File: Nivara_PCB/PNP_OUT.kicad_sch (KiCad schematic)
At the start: 16 parts, among them Q3 IRLML0040, Q4 IRLML0040, U10 LTV-357T, U11 LTV-357T

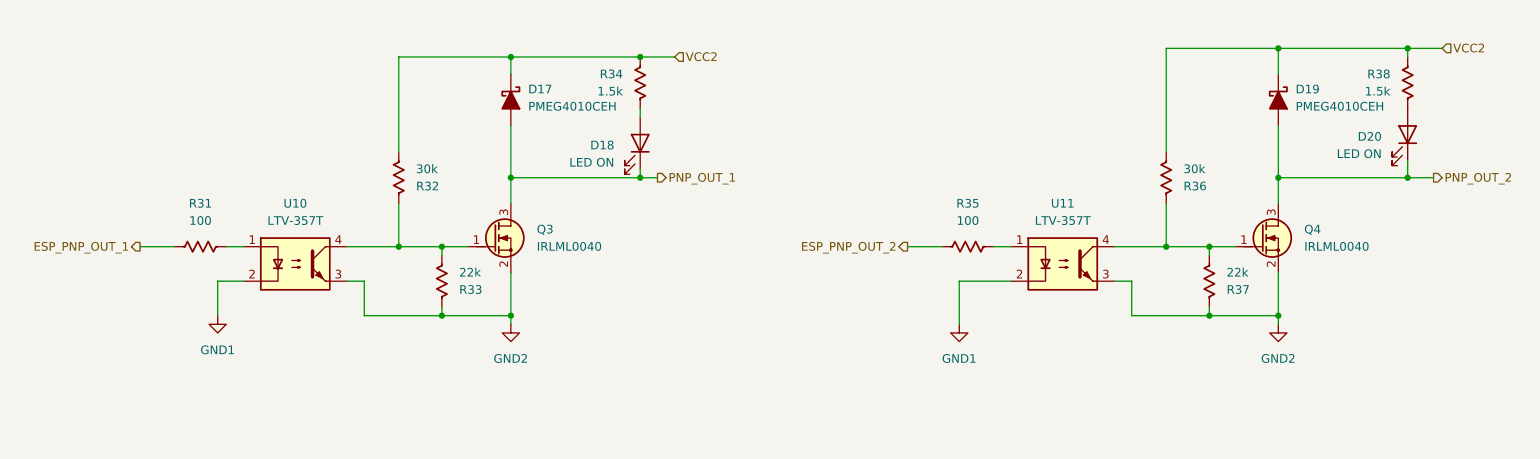
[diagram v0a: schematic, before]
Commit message: Cambios realizados en el PCB y el esquema de Nivara_PCB.
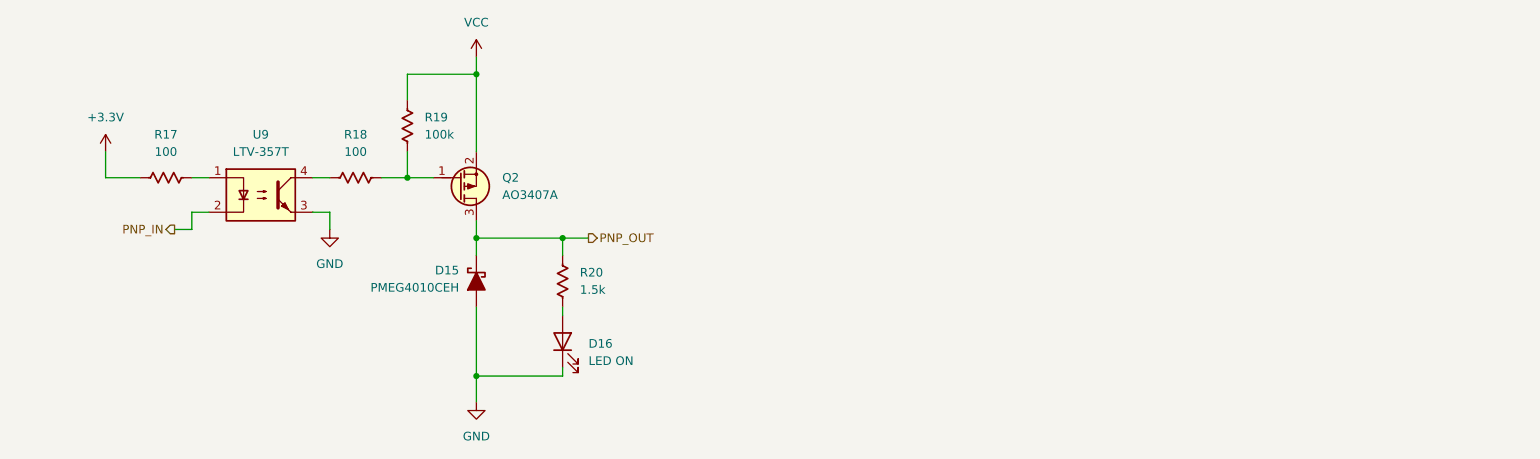
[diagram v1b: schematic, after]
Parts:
- removed D17, D19: PMEG4010CEH, PCM_Diode_SMD_AKL:D_SOD-123F, symbol PCM_Diode_Schottky_AKL:PMEG4010CEH
- removed D18, D20: LED ON, LED_SMD:LED_0603_1608Metric, symbol Device:LED
- removed Q3, Q4: IRLML0040, PCM_Package_TO_SOT_SMD_AKL:SOT-23, symbol PCM_Transistor_MOSFET_AKL:IRLML0040
- removed R31, R35: 100, PCM_Resistor_SMD_AKL:R_0603_1608Metric, symbol PCM_Resistor_US_AKL:R_0603
- removed R32, R36: 30k, PCM_Resistor_SMD_AKL:R_0603_1608Metric, symbol PCM_Resistor_US_AKL:R_0603
- removed R33, R37: 22k, PCM_Resistor_SMD_AKL:R_0603_1608Metric, symbol PCM_Resistor_US_AKL:R_0603
- removed R34, R38: 1.5k, PCM_Resistor_SMD_AKL:R_0603_1608Metric, symbol PCM_Resistor_US_AKL:R_0603
- removed U10, U11: LTV-357T, Package_SO:SO-4_4.4x3.6mm_P2.54mm, symbol Isolator:LTV-357T
- added D15: PMEG4010CEH, PCM_Diode_SMD_AKL:D_SOD-123F, symbol PCM_Diode_Schottky_AKL:PMEG4010CEH
- added D16: LED ON, LED_SMD:LED_0603_1608Metric, symbol Device:LED
- added Q2: AO3407A, PCM_Package_TO_SOT_SMD_AKL:SOT-23, symbol PCM_Transistor_MOSFET_AKL:AO3407A
- added R17, R18: 100, PCM_Resistor_SMD_AKL:R_0603_1608Metric, symbol PCM_Resistor_US_AKL:R_0603
- added R19: 100k, PCM_Resistor_SMD_AKL:R_0603_1608Metric, symbol PCM_Resistor_US_AKL:R_0603
- added R20: 1.5k, PCM_Resistor_SMD_AKL:R_0603_1608Metric, symbol PCM_Resistor_US_AKL:R_0603
- added U9: LTV-357T, Package_SO:SO-4_4.4x3.6mm_P2.54mm, symbol Isolator:LTV-357T
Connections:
- new net: Q2.1 (G), R18.1, R19.2
- new net: R18.2, U9.4
- new net: D16.2 (A), R20.2
- new net: R17.2, U9.1
- new net +3.3V: R17.1
- new net GND: D15.2 (A), D16.1 (K), U9.3
- new net PNP_IN: U9.2
- new net PNP_OUT: D15.1 (K), Q2.3 (D), R20.1
- new net VCC: Q2.2 (S), R19.1

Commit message: Cambios realizados en los archivos de Nivara_PCB.
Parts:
- D15: symbol PCM_Diode_Schottky_AKL:PMEG4010CEH -> EasyEDA:PMEG4010CEH
- D16: symbol Device:LED -> EasyEDA:LED
- Q2: symbol PCM_Transistor_MOSFET_AKL:AO3407A -> EasyEDA:AO3407A
- R17, R18, R19, R20: symbol PCM_Resistor_US_AKL:R_0603 -> EasyEDA:R_0603
- U9: symbol Isolator:LTV-357T -> EasyEDA:LTV-357T
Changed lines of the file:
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@@
 	)
 	(symbol
-		(lib_id "PCM_Diode_Schottky_AKL:PMEG4010CEH")
+		(lib_id "EasyEDA:PMEG4010CEH")
 		(at 100.33 90.17 270)
 		(mirror x)
@@
 	)
 	(symbol
-		(lib_id "power:+3.3V")
+		(lib_id "EasyEDA:+3.3V")
 		(at 45.72 71.12 0)
 		(unit 1)
@@
 	)
 	(symbol
-		(lib_id "PCM_Resistor_US_AKL:R_0603")
+		(lib_id "EasyEDA:R_0603")
 		(at 82.55 74.93 270)
 		(unit 1)
@@
 	)
 	(symbol
-		(lib_id "power:GND")
+		(lib_id "EasyEDA:GND")
 		(at 100.33 107.95 0)
 		(unit 1)
@@
 	)
 	(symbol
-		(lib_id "power:GND")
+		(lib_id "EasyEDA:GND")
 		(at 78.74 82.55 0)
 		(unit 1)
@@
 	)
 	(symbol
-		(lib_id "Device:LED")
+		(lib_id "EasyEDA:LED")
 		(at 113.03 99.06 90)
 		(unit 1)
@@
 	)
 	(symbol
-		(lib_id "PCM_Transistor_MOSFET_AKL:AO3407A")
+		(lib_id "EasyEDA:AO3407A")
 		(at 97.79 76.2 0)
 		(unit 1)
@@
 	)
 	(symbol
-		(lib_id "Isolator:LTV-357T")
+		(lib_id "EasyEDA:LTV-357T")
 		(at 68.58 77.47 0)
 		(unit 1)
@@
 	)
 	(symbol
-		(lib_id "power:VCC")
+		(lib_id "EasyEDA:VCC")
 		(at 100.33 57.15 0)
 		(unit 1)
@@
 	)
 	(symbol
-		(lib_id "PCM_Resistor_US_AKL:R_0603")
+		(lib_id "EasyEDA:R_0603")
 		(at 90.17 67.31 0)
 		(unit 1)
@@
 	)
 	(symbol
-		(lib_id "PCM_Resistor_US_AKL:R_0603")
+		(lib_id "EasyEDA:R_0603")
 		(at 54.61 74.93 90)
 		(unit 1)
@@
 	)
 	(symbol
-		(lib_id "PCM_Resistor_US_AKL:R_0603")
+		(lib_id "EasyEDA:R_0603")
 		(at 113.03 90.17 0)
 		(unit 1)
